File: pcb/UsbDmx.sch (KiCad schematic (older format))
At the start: 39 parts, among them CON101 10PIN_ISP_AVR, J101 Barrel_Jack, J102 USB_B, U101 L7805, U102 ATMEGA8515-16AU, U103 USBN9604-28M, U104 AS6C6264, U105 74LS573, Y101 24MHz

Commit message: Started footprint association
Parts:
- added C?: 100n, Capacitors_SMD:C_0603_HandSoldering, symbol device:C
- C101: value 100n 2kV -> 100n; footprint (none) -> Capacitors_SMD:C_0805_HandSoldering
- C103: footprint (none) -> Capacitors_THT:CP_Radial_D10.0mm_P5.00mm
- C105: footprint (none) -> Capacitors_SMD:C_0805_HandSoldering
- C110: footprint (none) -> Capacitors_THT:CP_Radial_D6.3mm_P2.50mm
- C113: footprint (none) -> Capacitors_THT:CP_Radial_D4.0mm_P1.50mm
- J101: footprint (none) -> proz_connectors:BARREL_JACK_CLIFF
- R101, R102, R103, R104, R105, R106, R107, R108, R109: footprint (none) -> Resistors_SMD:R_0603_HandSoldering
- Y101: footprint (none) -> Crystals:Crystal_HC49-U_Vertical
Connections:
- net GND: now also C?.2
- net at C113.1, R109.1, U103.18 (V3.3): now also C?.1
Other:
- moved on the sheet: C112
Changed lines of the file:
@@
 F 0 "R105" V 1450 1950 50  0000 C CNN
 F 1 "22" V 1550 2000 50  0000 C CNN
-F 2 "" V 1480 2000 50  0001 C CNN
+F 2 "Resistors_SMD:R_0603_HandSoldering" V 1480 2000 50  0001 C CNN
 F 3 "~" H 1550 2000 50  0001 C CNN
 	1    1550 2000
@@
 F 0 "R106" V 1650 2050 50  0000 C CNN
 F 1 "22" V 1550 2100 50  0000 C CNN
-F 2 "" V 1480 2100 50  0001 C CNN
+F 2 "Resistors_SMD:R_0603_HandSoldering" V 1480 2100 50  0001 C CNN
 F 3 "~" H 1550 2100 50  0001 C CNN
 	1    1550 2100
@@
 F 0 "R109" V 2600 2350 50  0000 C CNN
 F 1 "1k5" V 2700 2400 50  0000 C CNN
-F 2 "" V 2630 2400 50  0001 C CNN
+F 2 "Resistors_SMD:R_0603_HandSoldering" V 2630 2400 50  0001 C CNN
 F 3 "~" H 2700 2400 50  0001 C CNN
 	1    2700 2400
@@
 F 0 "C113" H 4268 2896 50  0000 L CNN
 F 1 "1u" H 4268 2805 50  0000 L CNN
-F 2 "" H 4188 2700 50  0001 C CNN
+F 2 "Capacitors_THT:CP_Radial_D4.0mm_P1.50mm" H 4188 2700 50  0001 C CNN
 F 3 "~" H 4150 2850 50  0001 C CNN
 	1    4150 2850
@@
 Connection ~ 4150 2400
 Wire Wire Line
-	4150 2400 2850 2400
+	4150 2400 3800 2400
 $Comp
 L proz_ram:AS6C6264 U104
@@
 F 0 "Y101" V 3454 1381 50  0000 L CNN
 F 1 "24MHz" V 3545 1381 50  0000 L CNN
-F 2 "" H 3500 1250 50  0001 C CNN
+F 2 "Crystals:Crystal_HC49-U_Vertical" H 3500 1250 50  0001 C CNN
 F 3 "~" H 3500 1250 50  0001 C CNN
 	1    3500 1250
@@
 F 0 "J101" H 828 4175 50  0000 C CNN
 F 1 "Barrel_Jack" H 828 4084 50  0000 C CNN
-F 2 "" H 800 3810 50  0001 C CNN
+F 2 "proz_connectors:BARREL_JACK_CLIFF" H 800 3810 50  0001 C CNN
 F 3 "~" H 800 3810 50  0001 C CNN
 	1    750  3850
@@
 L power:+5V #PWR0121
 U 1 1 5BFD5DB3
-P 3650 3450
-F 0 "#PWR0121" H 3650 3300 50  0001 C CNN
-F 1 "+5V" H 3665 3623 50  0000 C CNN
-F 2 "" H 3650 3450 50  0001 C CNN
-F 3 "" H 3650 3450 50  0001 C CNN
-	1    3650 3450
+P 3600 3450
+F 0 "#PWR0121" H 3600 3300 50  0001 C CNN
+F 1 "+5V" H 3615 3623 50  0000 C CNN
+F 2 "" H 3600 3450 50  0001 C CNN
+F 3 "" H 3600 3450 50  0001 C CNN
+	1    3600 3450
 	1    0    0    -1
 $EndComp
@@
 	1250 3950 1250 3850
 Wire Wire Line
-	3650 3450 3650 3750
-Wire Wire Line
-	3650 3750 3550 3750
+	3600 3450 3600 3750
+Wire Wire Line
+	3600 3750 3550 3750
 Text Label 2850 3350 0    50   ~ 0
 5V_EXT
@@
 F 0 "R101" V 800 5050 50  0000 C CNN
 F 1 "10k" V 900 5100 50  0000 C CNN
-F 2 "" V 830 5100 50  0001 C CNN
+F 2 "Resistors_SMD:R_0603_HandSoldering" V 830 5100 50  0001 C CNN
 F 3 "~" H 900 5100 50  0001 C CNN
 	1    900  5100
@@
 F 0 "R103" V 1400 5050 50  0000 C CNN
 F 1 "2k2" V 1500 5100 50  0000 C CNN
-F 2 "" V 1430 5100 50  0001 C CNN
+F 2 "Resistors_SMD:R_0603_HandSoldering" V 1430 5100 50  0001 C CNN
 F 3 "~" H 1500 5100 50  0001 C CNN
 	1    1500 5100
@@
 F 0 "R104" V 1400 5550 50  0000 C CNN
 F 1 "47k" V 1500 5600 50  0000 C CNN
-F 2 "" V 1430 5600 50  0001 C CNN
+F 2 "Resistors_SMD:R_0603_HandSoldering" V 1430 5600 50  0001 C CNN
 F 3 "~" H 1500 5600 50  0001 C CNN
 	1    1500 5600
@@
 F 0 "R107" V 2150 5050 50  0000 C CNN
 F 1 "2k2" V 2250 5100 50  0000 C CNN
-F 2 "" V 2180 5100 50  0001 C CNN
+F 2 "Resistors_SMD:R_0603_HandSoldering" V 2180 5100 50  0001 C CNN
 F 3 "~" H 2250 5100 50  0001 C CNN
 	1    2250 5100
@@
 F 0 "R108" V 2150 5550 50  0000 C CNN
 F 1 "47k" V 2250 5600 50  0000 C CNN
-F 2 "" V 2180 5600 50  0001 C CNN
+F 2 "Resistors_SMD:R_0603_HandSoldering" V 2180 5600 50  0001 C CNN
 F 3 "~" H 2250 5600 50  0001 C CNN
 	1    2250 5600
@@
 F 0 "C103" H 1700 4100 50  0000 L CNN
 F 1 "470u" H 1450 3900 50  0000 L CNN
-F 2 "" H 1688 3850 50  0001 C CNN
+F 2 "Capacitors_THT:CP_Radial_D10.0mm_P5.00mm" H 1688 3850 50  0001 C CNN
 F 3 "~" H 1650 4000 50  0001 C CNN
 	1    1650 4000
@@
 F 0 "C105" H 2000 4100 50  0000 L CNN
 F 1 "100n" H 1750 3900 50  0000 L CNN
-F 2 "" H 1988 3850 50  0001 C CNN
+F 2 "Capacitors_SMD:C_0805_HandSoldering" H 1988 3850 50  0001 C CNN
 F 3 "~" H 1950 4000 50  0001 C CNN
 	1    1950 4000
@@
 F 0 "C110" H 3200 4100 50  0000 L CNN
 F 1 "100u" H 2950 3900 50  0000 L CNN
-F 2 "" H 3188 3850 50  0001 C CNN
+F 2 "Capacitors_THT:CP_Radial_D6.3mm_P2.50mm" H 3188 3850 50  0001 C CNN
 F 3 "~" H 3150 4000 50  0001 C CNN
 	1    3150 4000
@@
 F 0 "R102" V 1100 850 50  0000 C CNN
 F 1 "100" V 1150 700 50  0000 C CNN
-F 2 "" V 1080 700 50  0001 C CNN
+F 2 "Resistors_SMD:R_0603_HandSoldering" V 1080 700 50  0001 C CNN
 F 3 "~" H 1150 700 50  0001 C CNN
 	1    1150 700
@@
 L device:C C112
 U 1 1 5C820162
-P 3850 2850
-F 0 "C112" H 3900 2950 50  0000 L CNN
-F 1 "100n" H 3650 2750 50  0000 L CNN
-F 2 "Capacitors_SMD:C_0603_HandSoldering" H 3888 2700 50  0001 C CNN
-F 3 "~" H 3850 2850 50  0001 C CNN
-	1    3850 2850
+P 3450 2850
+F 0 "C112" H 3500 2950 50  0000 L CNN
+F 1 "100n" H 3250 2750 50  0000 L CNN
+F 2 "Capacitors_SMD:C_0603_HandSoldering" H 3488 2700 50  0001 C CNN
+F 3 "~" H 3450 2850 50  0001 C CNN
+	1    3450 2850
 	1    0    0    -1
 $EndComp
@@
 L power:GND #PWR0122
 U 1 1 5C8203C8
-P 3850 3100
-F 0 "#PWR0122" H 3850 2850 50  0001 C CNN
-F 1 "GND" H 3855 2927 50  0000 C CNN
-F 2 "" H 3850 3100 50  0001 C CNN
-F 3 "" H 3850 3100 50  0001 C CNN
-	1    3850 3100
-	1    0    0    -1
-$EndComp
-Wire Wire Line
-	3850 3100 3850 3000
-Wire Wire Line
-	3850 2700 3850 2300
-Wire Wire Line
-	3850 2300 4150 2300
+P 3450 3100
+F 0 "#PWR0122" H 3450 2850 50  0001 C CNN
+F 1 "GND" H 3455 2927 50  0000 C CNN
+F 2 "" H 3450 3100 50  0001 C CNN
+F 3 "" H 3450 3100 50  0001 C CNN
+	1    3450 3100
+	1    0    0    -1
+$EndComp
+Wire Wire Line
+	3450 3100 3450 3000
+Wire Wire Line
+	3450 2700 3450 2300
+Wire Wire Line
+	3450 2300 4150 2300
 Connection ~ 4150 2300
 NoConn ~ 7800 2000
@@
 P 850 2650
 F 0 "C101" V 600 2600 50  0000 L CNN
-F 1 "100n 2kV" V 700 2500 50  0000 L CNN
-F 2 "" H 888 2500 50  0001 C CNN
+F 1 "100n" V 700 2500 50  0000 L CNN
+F 2 "Capacitors_SMD:C_0805_HandSoldering" H 888 2500 50  0001 C CNN
 F 3 "~" H 850 2650 50  0001 C CNN
 	1    850  2650
@@
 Wire Wire Line
 	900  2900 850  2900
+$Comp
+L device:C C?
+U 1 1 5BFDF482
+P 3800 2850
+F 0 "C?" H 3850 2950 50  0000 L CNN
+F 1 "100n" H 3600 2750 50  0000 L CNN
+F 2 "Capacitors_SMD:C_0603_HandSoldering" H 3838 2700 50  0001 C CNN
+F 3 "~" H 3800 2850 50  0001 C CNN
+	1    3800 2850
+	1    0    0    -1
+$EndComp
+$Comp
+L power:GND #PWR?
+U 1 1 5C0135A2
+P 3800 3100
+F 0 "#PWR?" H 3800 2850 50  0001 C CNN
+F 1 "GND" H 3805 2927 50  0000 C CNN
+F 2 "" H 3800 3100 50  0001 C CNN
+F 3 "" H 3800 3100 50  0001 C CNN
+	1    3800 3100
+	1    0    0    -1
+$EndComp
+Wire Wire Line
+	3800 2700 3800 2400
+Connection ~ 3800 2400
+Wire Wire Line
+	3800 2400 2850 2400
+Wire Wire Line
+	3800 3000 3800 3100
 Wire Bus Line
 	10350 1650 10350 3350

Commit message: finished footprint association
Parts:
- added C117: 100n, Capacitors_SMD:C_0805_HandSoldering, symbol device:C
- added U106: USBLC6-2SC6, TO_SOT_Packages_SMD:SOT-23-6, symbol ESD_Protection:USBLC6-2SC6
- D101: footprint (none) -> proz_led:LED_SMD_0603
- gave numbers to parts that had none: 1
- renumbered C115 to C101, C108 to C102, C109 to C103, C101 to C104, C114 to C105, C112 to C106, C113 to C108, C103 to C109, C105 to C110, C107 to C111, C110 to C112, C102 to C113, C104 to C114, C106 to C115, C111 to C116, D103 to D102, D104 to D103, D102 to D104, J102 to J101, J101 to J102, R102 to R101, R105 to R102, R106 to R103, R109 to R104, R101 to R105, R103 to R106, R104 to R108, R108 to R109, U105 to U101, U103 to U102, U104 to U103, U101 to U104, U102 to U105
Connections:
- net 5V_USB: now also C117.1, U106.5 (VBUS)
- net GND: now also C117.2, U106.2 (GND)
- net at R102.1, R104.2, U102.19 (D+): now also U106.3 (IO2), U106.4 (IO2)
- net at R103.1, U102.20 (D-): now also U106.1 (IO1), U106.6 (IO1)
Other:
- moved on the sheet: F101, R102, R103, R104

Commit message: startet layouting
Startet to create a Layout
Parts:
- added L101: 1271.1001, proz_unknown:1271.1001, symbol proz_util:LightLine
- added R110: 1M, Resistors_SMD:R_0603_HandSoldering, symbol device:R
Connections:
- net A0: now also U101.12 (Q7); no longer U101.19 (Q0)
- net A1: now also U101.13 (Q6); no longer U101.18 (Q1)
- net A2: now also U101.14 (Q5); no longer U101.17 (Q2)
- net A3: now also U101.15 (Q4); no longer U101.16 (Q3)
- net A4: now also U101.16 (Q3); no longer U101.15 (Q4)
- net A5: now also U101.17 (Q2); no longer U101.14 (Q5)
- net A6: now also U101.18 (Q1); no longer U101.13 (Q6)
- net A7: now also U101.19 (Q0); no longer U101.12 (Q7)
- net AD0: now also U101.9 (D7); no longer U101.2 (D0)
- net AD1: now also U101.8 (D6); no longer U101.3 (D1)
- net AD2: now also U101.7 (D5); no longer U101.4 (D2)
- net AD3: now also U101.6 (D4); no longer U101.5 (D3)
- net AD4: now also U101.5 (D3); no longer U101.6 (D4)
- net AD5: now also U101.4 (D2); no longer U101.7 (D5)
- net AD6: now also U101.3 (D1); no longer U101.8 (D6)
- net AD7: now also U101.2 (D0); no longer U101.9 (D7)
- net at C103.1, U102.26 (XIN), Y101.2: now also R110.2
- net at C102.1, U102.27 (XOUT), Y101.1: now also R110.1
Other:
- moved on the sheet: Y101
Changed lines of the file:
@@
 L device:Crystal Y101
 U 1 1 5BF9C616
-P 3500 1250
-F 0 "Y101" V 3454 1381 50  0000 L CNN
-F 1 "24MHz" V 3545 1381 50  0000 L CNN
-F 2 "Crystals:Crystal_HC49-U_Vertical" H 3500 1250 50  0001 C CNN
-F 3 "~" H 3500 1250 50  0001 C CNN
-	1    3500 1250
+P 3400 1250
+F 0 "Y101" V 3250 1300 50  0000 L CNN
+F 1 "24MHz" V 3550 1300 50  0000 L CNN
+F 2 "Crystals:Crystal_HC49-U_Vertical" H 3400 1250 50  0001 C CNN
+F 3 "~" H 3400 1250 50  0001 C CNN
+	1    3400 1250
 	0    1    1    0
 $EndComp
@@
 $EndComp
 Wire Wire Line
-	4550 1300 3950 1300
-Wire Wire Line
-	3950 1300 3950 1450
-Wire Wire Line
-	3950 1450 3500 1450
-Wire Wire Line
-	3500 1450 3500 1400
-Wire Wire Line
-	3300 1450 3500 1450
-Connection ~ 3500 1450
-Wire Wire Line
-	3300 1050 3500 1050
-Wire Wire Line
-	3950 1050 3950 1200
-Wire Wire Line
-	3950 1200 4550 1200
-Wire Wire Line
-	3500 1100 3500 1050
-Connection ~ 3500 1050
-Wire Wire Line
-	3500 1050 3950 1050
+	4550 1300 4000 1300
+Wire Wire Line
+	4000 1300 4000 1450
+Wire Wire Line
+	4000 1450 3750 1450
+Wire Wire Line
+	3400 1450 3400 1400
+Wire Wire Line
+	3300 1450 3400 1450
+Connection ~ 3400 1450
+Wire Wire Line
+	3300 1050 3400 1050
+Wire Wire Line
+	4000 1050 4000 1200
+Wire Wire Line
+	4000 1200 4550 1200
+Wire Wire Line
+	3400 1100 3400 1050
+Connection ~ 3400 1050
+Wire Wire Line
+	3400 1050 3750 1050
 Wire Wire Line
 	3000 1450 2900 1450
@@
 Text Label 8000 1800 0    50   ~ 0
 AD7
+Text Label 8600 2250 0    50   ~ 0
+AD0
+Text Label 8600 2150 0    50   ~ 0
+AD1
+Text Label 8600 2050 0    50   ~ 0
+AD2
+Text Label 8600 1950 0    50   ~ 0
+AD3
+Text Label 8600 1850 0    50   ~ 0
+AD4
+Text Label 8600 1750 0    50   ~ 0
+AD5
+Text Label 8600 1650 0    50   ~ 0
+AD6
 Text Label 8600 1550 0    50   ~ 0
-AD0
-Text Label 8600 1650 0    50   ~ 0
-AD1
-Text Label 8600 1750 0    50   ~ 0
-AD2
-Text Label 8600 1850 0    50   ~ 0
-AD3
-Text Label 8600 1950 0    50   ~ 0
-AD4
-Text Label 8600 2050 0    50   ~ 0
-AD5
-Text Label 8600 2150 0    50   ~ 0
-AD6
-Text Label 8600 2250 0    50   ~ 0
 AD7
-Text Label 9950 1550 0    50   ~ 0
+Text Label 9900 2250 0    50   ~ 0
 A0
-Text Label 9950 1650 0    50   ~ 0
+Text Label 9900 2150 0    50   ~ 0
 A1
-Text Label 9950 1750 0    50   ~ 0
+Text Label 9900 2050 0    50   ~ 0
 A2
-Text Label 9950 1850 0    50   ~ 0
+Text Label 9900 1950 0    50   ~ 0
 A3
-Text Label 9950 1950 0    50   ~ 0
+Text Label 9900 1850 0    50   ~ 0
 A4
-Text Label 9950 2050 0    50   ~ 0
+Text Label 9900 1750 0    50   ~ 0
 A5
-Text Label 9950 2150 0    50   ~ 0
+Text Label 9900 1650 0    50   ~ 0
 A6
-Text Label 9950 2250 0    50   ~ 0
+Text Label 9900 1550 0    50   ~ 0
 A7
 $Comp
@@
 Wire Wire Line
 	1550 2350 1750 2350
+Connection ~ 1750 2350
+Wire Wire Line
+	1750 2350 1750 1800
+$Comp
+L proz_util:LightLine L?
+U 1 1 5C1BA6D0
+P 800 650
+AR Path="/5C0322AA/5C1BA6D0" Ref="L?"  Part="1"
+AR Path="/5C1BA6D0" Ref="L101"  Part="1"
+F 0 "L101" H 600 650 50  0000 R CNN
+F 1 "1271.1001" H 1100 750 50  0000 R CNN
+F 2 "proz_unknown:1271.1001" H 800 650 50  0001 C CNN
+F 3 "" H 800 650 50  0001 C CNN
+	1    800  650
+	1    0    0    -1
+$EndComp
+$Comp
+L device:R R110
+U 1 1 5C211C9C
+P 3750 1250
+F 0 "R110" H 3820 1296 50  0000 L CNN
+F 1 "1M" H 3820 1205 50  0000 L CNN
+F 2 "Resistors_SMD:R_0603_HandSoldering" V 3680 1250 50  0001 C CNN
+F 3 "~" H 3750 1250 50  0001 C CNN
+	1    3750 1250
+	1    0    0    -1
+$EndComp
+Wire Wire Line
+	3750 1100 3750 1050
+Connection ~ 3750 1050
+Wire Wire Line
+	3750 1050 4000 1050
+Wire Wire Line
+	3750 1400 3750 1450
+Connection ~ 3750 1450
+Wire Wire Line
+	3750 1450 3400 1450
 Wire Bus Line
 	10350 1650 10350 3350
@@
 Wire Bus Line
 	6350 1500 6350 5950
-Connection ~ 1750 2350
-Wire Wire Line
-	1750 2350 1750 1800
 $EndSCHEMATC

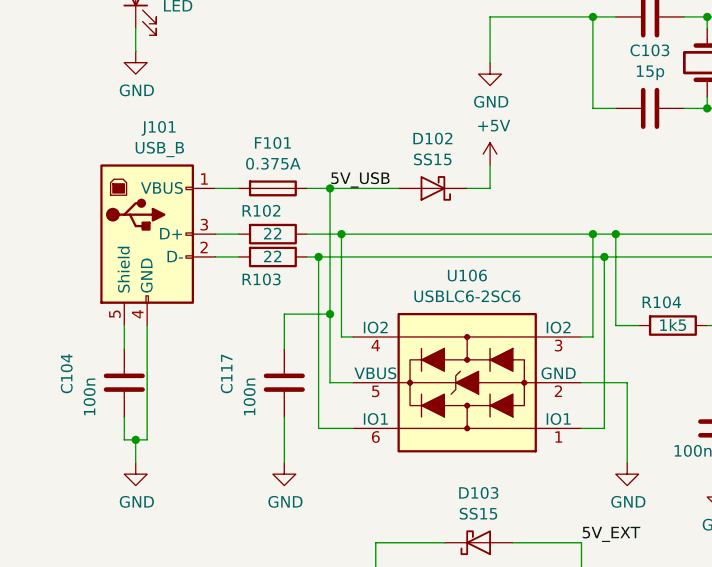
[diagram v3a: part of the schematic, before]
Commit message: Finished layout
Added esd protection diodes to the dmx interface
Routed everything
added ground planes
added some logos...
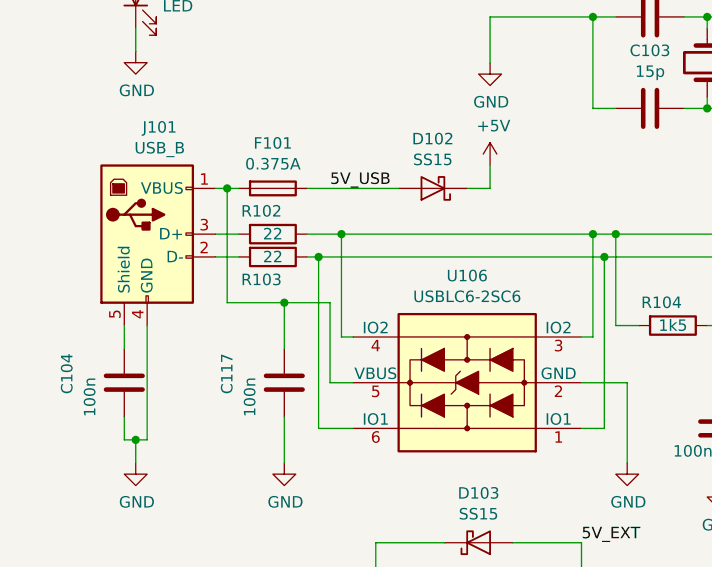
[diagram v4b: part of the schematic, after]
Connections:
- net 5V_USB: no longer C117.1, U106.5 (VBUS)
- net at F101.2, J101.1 (VBUS): now also C117.1, U106.5 (VBUS)
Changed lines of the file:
@@
 $EndComp
 Wire Wire Line
-	1350 1800 1250 1800
+	1350 1800 1300 1800
 $Comp
 L diode:SB150 D102
@@
 	-1   0    0    1
 $EndComp
-Wire Wire Line
-	2050 1800 1750 1800
 Text Label 1750 1800 0    50   ~ 0
 5V_USB
@@
 Wire Wire Line
 	1850 2650 1750 2650
-Wire Wire Line
-	1750 2650 1750 2350
-Connection ~ 1750 1800
-Wire Wire Line
-	1750 1800 1650 1800
 $Comp
 L power:GND #PWR0140
@@
 Wire Wire Line
 	1550 3000 1550 2800
-Wire Wire Line
-	1550 2500 1550 2350
-Wire Wire Line
-	1550 2350 1750 2350
-Connection ~ 1750 2350
-Wire Wire Line
-	1750 2350 1750 1800
 $Comp
 L proz_util:LightLine L?
@@
 Wire Wire Line
 	3750 1450 3400 1450
+Wire Wire Line
+	1750 2650 1750 2300
+Wire Wire Line
+	1750 2300 1550 2300
+Wire Wire Line
+	1300 2300 1300 1800
+Connection ~ 1300 1800
+Wire Wire Line
+	1300 1800 1250 1800
+Wire Wire Line
+	1650 1800 2050 1800
+Wire Wire Line
+	1550 2500 1550 2300
+Connection ~ 1550 2300
+Wire Wire Line
+	1550 2300 1300 2300
 Wire Bus Line
 	10350 1650 10350 3350

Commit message: final release 1.0
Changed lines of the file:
@@
 AR Path="/5C0322AA/5C1BA6D0" Ref="L?"  Part="1"
 AR Path="/5C1BA6D0" Ref="L101"  Part="1"
-F 0 "L101" H 600 650 50  0000 R CNN
+F 0 "L101" H 850 500 50  0000 R CNN
 F 1 "1271.1001" H 1100 750 50  0000 R CNN
 F 2 "proz_unknown:1271.1001" H 800 650 50  0001 C CNN
